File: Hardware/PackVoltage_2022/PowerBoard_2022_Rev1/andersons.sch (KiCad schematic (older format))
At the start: 22 parts

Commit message: Actuation shit
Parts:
- removed unit 3 of Conn2
- removed Conn23: AndersonPP, MRDT_Connectors:Anderson_3_Horizontal_Side_by_Side, symbol PowerBoard_2022_Rev1-rescue:AndersonPP-MRDT_Connectors
- removed unit 3 of Conn3
- removed unit 3 of Conn4
- removed unit 3 of Conn5
- removed unit 3 of Conn6
- removed unit 3 of Conn7
- removed unit 3 of Conn9
- added Conn13: AndersonPP-MRDT_Connectors, MRDT_Connectors:Anderson_3_Horizontal_Side_by_Side, symbol PowerBoard_2022_Rev1-rescue:AndersonPP-MRDT_Connectors
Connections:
- net labels added: Anderson_GimAct, Anderson_SciAct
- net labels removed: Anderson_SciLog
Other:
- moved on the sheet: Conn1C, Conn20A, Conn22B, Conn3A, Conn4A, Conn8C

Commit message: Made it to layout, found out about gnd via
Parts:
- removed Conn13, Conn22: AndersonPP-MRDT_Connectors, MRDT_Connectors:Anderson_3_Horizontal_Side_by_Side, symbol PowerBoard_2022_Rev1-rescue:AndersonPP-MRDT_Connectors
- added unit 2 of Conn11
- added unit 2 of Conn17
- added unit 2 of Conn18
- added unit 2 of Conn19
- added unit 2 of Conn20
- added unit 2 of Conn3
- added unit 2 of Conn4
- added unit 2 of Conn7
- added unit 2 of Conn8
- Conn1, Conn10, Conn11, Conn14, Conn18, Conn4, Conn6, Conn7, Conn8: footprint MRDT_Connectors:Anderson_3_Horizontal_Side_by_Side -> MRDT_Connectors:Anderson_2_Vertical_Sidy_by_Side
- Conn10: renamed from Conn16; footprint MRDT_Connectors:Anderson_3_Horizontal_Side_by_Side -> MRDT_Connectors:Anderson_2_Vertical_Sidy_by_Side
- Conn12, Conn14: renamed from Conn9; footprint MRDT_Connectors:Anderson_3_Horizontal_Side_by_Side -> MRDT_Connectors:Anderson_2_Vertical_Sidy_by_Side
- Conn12, Conn9: renamed from Conn5; footprint MRDT_Connectors:Anderson_3_Horizontal_Side_by_Side -> MRDT_Connectors:Anderson_2_Vertical_Sidy_by_Side
- Conn13, Conn16: renamed from Conn12; footprint MRDT_Connectors:Anderson_3_Horizontal_Side_by_Side -> MRDT_Connectors:Anderson_2_Vertical_Sidy_by_Side
- Conn13: renamed from Conn7; footprint MRDT_Connectors:Anderson_3_Horizontal_Side_by_Side -> MRDT_Connectors:Anderson_2_Vertical_Sidy_by_Side
- Conn15: renamed from Conn17; footprint MRDT_Connectors:Anderson_3_Horizontal_Side_by_Side -> MRDT_Connectors:Anderson_2_Vertical_Sidy_by_Side
- Conn15: renamed from Conn11; footprint MRDT_Connectors:Anderson_3_Horizontal_Side_by_Side -> MRDT_Connectors:Anderson_2_Vertical_Sidy_by_Side
- Conn16: renamed from Conn19; footprint MRDT_Connectors:Anderson_3_Horizontal_Side_by_Side -> MRDT_Connectors:Anderson_2_Vertical_Sidy_by_Side
- Conn17: renamed from Conn15; footprint MRDT_Connectors:Anderson_3_Horizontal_Side_by_Side -> MRDT_Connectors:Anderson_2_Vertical_Sidy_by_Side
- Conn19: renamed from Conn20; footprint MRDT_Connectors:Anderson_3_Horizontal_Side_by_Side -> MRDT_Connectors:Anderson_3_Vertical_Side_by_Side
- Conn19: renamed from Conn8; footprint MRDT_Connectors:Anderson_3_Horizontal_Side_by_Side -> MRDT_Connectors:Anderson_3_Vertical_Side_by_Side
- Conn2: renamed from Conn6; footprint MRDT_Connectors:Anderson_3_Horizontal_Side_by_Side -> MRDT_Connectors:Anderson_2_Vertical_Sidy_by_Side
- Conn2: renamed from Conn4; footprint MRDT_Connectors:Anderson_3_Horizontal_Side_by_Side -> MRDT_Connectors:Anderson_2_Vertical_Sidy_by_Side
- Conn20: renamed from Conn21; footprint MRDT_Connectors:Anderson_3_Horizontal_Side_by_Side -> MRDT_Connectors:Anderson_2_Vertical_Sidy_by_Side
- Conn3: footprint MRDT_Connectors:Anderson_3_Horizontal_Side_by_Side -> MRDT_Connectors:Anderson_3_Vertical_Side_by_Side
- Conn3: renamed from Conn1; footprint MRDT_Connectors:Anderson_3_Horizontal_Side_by_Side -> MRDT_Connectors:Anderson_3_Vertical_Side_by_Side
- Conn5: renamed from Conn2; footprint MRDT_Connectors:Anderson_3_Horizontal_Side_by_Side -> MRDT_Connectors:Anderson_2_Vertical_Sidy_by_Side
- Conn6: renamed from Conn10; footprint MRDT_Connectors:Anderson_3_Horizontal_Side_by_Side -> MRDT_Connectors:Anderson_2_Vertical_Sidy_by_Side
- Conn9: renamed from Conn3; footprint MRDT_Connectors:Anderson_3_Horizontal_Side_by_Side -> MRDT_Connectors:Anderson_2_Vertical_Sidy_by_Side
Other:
- moved on the sheet: Conn10A, Conn10D, Conn12A, Conn12D, Conn13A, Conn13D, Conn14A, Conn14D, Conn15A, Conn15D, Conn16A, Conn16D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

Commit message: Revert "Placed Components for Motor 1 and fixed errors with netlist"
This reverts commit 86a32237b1b6d07fe668dfe10dac6f9ef44dc23b.
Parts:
- Conn1, Conn10, Conn12, Conn13, Conn14, Conn15, Conn16, Conn2, Conn5, Conn6, Conn9: footprint MRDT_Connectors:Anderson_2_Vertical_Sidy_by_Side -> MRDT_Connectors:Anderson_2_Vertical_Side_by_Side_PV
- Conn11, Conn17, Conn18, Conn19, Conn20, Conn3, Conn4, Conn7, Conn8: symbol MRDT_Connectors:AndersonPP -> PowerBoard_2022_Rev1-rescue:AndersonPP-MRDT_Connectors
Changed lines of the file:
@@
 EESchema Schematic File Version 4
-LIBS:PowerBoard_2022_Rev1-cache
-EELAYER 26 0
+EELAYER 30 0
 EELAYER END
 $Descr A4 11693 8268
@@
 F 0 "Conn1" H 808 1837 60  0000 C CNN
 F 1 "AndersonPP" H 808 1731 60  0000 C CNN
-F 2 "MRDT_Connectors:Anderson_2_Vertical_Sidy_by_Side" H 450 900 60  0001 C CNN
+F 2 "MRDT_Connectors:Anderson_2_Vertical_Side_by_Side_PV" H 450 900 60  0001 C CNN
 F 3 "" H 450 900 60  0001 C CNN
 	1    600  1450
@@
 F 0 "Conn1" H 808 1337 60  0000 C CNN
 F 1 "AndersonPP" H 808 1231 60  0000 C CNN
-F 2 "MRDT_Connectors:Anderson_2_Vertical_Sidy_by_Side" H 450 400 60  0001 C CNN
+F 2 "MRDT_Connectors:Anderson_2_Vertical_Side_by_Side_PV" H 450 400 60  0001 C CNN
 F 3 "" H 450 400 60  0001 C CNN
 	4    600  950
@@
 F 0 "Conn9" H 3108 1887 60  0000 C CNN
 F 1 "AndersonPP" H 3108 1781 60  0000 C CNN
-F 2 "MRDT_Connectors:Anderson_2_Vertical_Sidy_by_Side" H 2750 950 60  0001 C CNN
+F 2 "MRDT_Connectors:Anderson_2_Vertical_Side_by_Side_PV" H 2750 950 60  0001 C CNN
 F 3 "" H 2750 950 60  0001 C CNN
 	1    2900 1500
@@
 F 0 "Conn9" H 3108 1387 60  0000 C CNN
 F 1 "AndersonPP" H 3108 1281 60  0000 C CNN
-F 2 "MRDT_Connectors:Anderson_2_Vertical_Sidy_by_Side" H 2750 450 60  0001 C CNN
+F 2 "MRDT_Connectors:Anderson_2_Vertical_Side_by_Side_PV" H 2750 450 60  0001 C CNN
 F 3 "" H 2750 450 60  0001 C CNN
 	4    2900 1000
@@
 F 0 "Conn12" H 4208 1887 60  0000 C CNN
 F 1 "AndersonPP" H 4208 1781 60  0000 C CNN
-F 2 "MRDT_Connectors:Anderson_2_Vertical_Sidy_by_Side" H 3850 950 60  0001 C CNN
+F 2 "MRDT_Connectors:Anderson_2_Vertical_Side_by_Side_PV" H 3850 950 60  0001 C CNN
 F 3 "" H 3850 950 60  0001 C CNN
 	1    4000 1500
@@
 F 0 "Conn12" H 4208 1387 60  0000 C CNN
 F 1 "AndersonPP" H 4208 1281 60  0000 C CNN
-F 2 "MRDT_Connectors:Anderson_2_Vertical_Sidy_by_Side" H 3850 450 60  0001 C CNN
+F 2 "MRDT_Connectors:Anderson_2_Vertical_Side_by_Side_PV" H 3850 450 60  0001 C CNN
 F 3 "" H 3850 450 60  0001 C CNN
 	4    4000 1000
@@
 F 0 "Conn13" H 5258 1887 60  0000 C CNN
 F 1 "AndersonPP" H 5258 1781 60  0000 C CNN
-F 2 "MRDT_Connectors:Anderson_2_Vertical_Sidy_by_Side" H 4900 950 60  0001 C CNN
+F 2 "MRDT_Connectors:Anderson_2_Vertical_Side_by_Side_PV" H 4900 950 60  0001 C CNN
 F 3 "" H 4900 950 60  0001 C CNN
 	1    5050 1500
@@
 F 0 "Conn13" H 5258 1387 60  0000 C CNN
 F 1 "AndersonPP" H 5258 1281 60  0000 C CNN
-F 2 "MRDT_Connectors:Anderson_2_Vertical_Sidy_by_Side" H 4900 450 60  0001 C CNN
+F 2 "MRDT_Connectors:Anderson_2_Vertical_Side_by_Side_PV" H 4900 450 60  0001 C CNN
 F 3 "" H 4900 450 60  0001 C CNN
 	4    5050 1000
@@
 F 0 "Conn14" H 6458 1887 60  0000 C CNN
 F 1 "AndersonPP" H 6458 1781 60  0000 C CNN
-F 2 "MRDT_Connectors:Anderson_2_Vertical_Sidy_by_Side" H 6100 950 60  0001 C CNN
+F 2 "MRDT_Connectors:Anderson_2_Vertical_Side_by_Side_PV" H 6100 950 60  0001 C CNN
 F 3 "" H 6100 950 60  0001 C CNN
 	1    6250 1500
@@
 F 0 "Conn14" H 6458 1387 60  0000 C CNN
 F 1 "AndersonPP" H 6458 1281 60  0000 C CNN
-F 2 "MRDT_Connectors:Anderson_2_Vertical_Sidy_by_Side" H 6100 450 60  0001 C CNN
+F 2 "MRDT_Connectors:Anderson_2_Vertical_Side_by_Side_PV" H 6100 450 60  0001 C CNN
 F 3 "" H 6100 450 60  0001 C CNN
 	4    6250 1000
@@
 F 0 "Conn15" H 7608 1887 60  0000 C CNN
 F 1 "AndersonPP" H 7608 1781 60  0000 C CNN
-F 2 "MRDT_Connectors:Anderson_2_Vertical_Sidy_by_Side" H 7250 950 60  0001 C CNN
+F 2 "MRDT_Connectors:Anderson_2_Vertical_Side_by_Side_PV" H 7250 950 60  0001 C CNN
 F 3 "" H 7250 950 60  0001 C CNN
 	1    7400 1500
@@
 F 0 "Conn15" H 7608 1387 60  0000 C CNN
 F 1 "AndersonPP" H 7608 1281 60  0000 C CNN
-F 2 "MRDT_Connectors:Anderson_2_Vertical_Sidy_by_Side" H 7250 450 60  0001 C CNN
+F 2 "MRDT_Connectors:Anderson_2_Vertical_Side_by_Side_PV" H 7250 450 60  0001 C CNN
 F 3 "" H 7250 450 60  0001 C CNN
 	4    7400 1000
@@
 F 0 "Conn16" H 8858 1887 60  0000 C CNN
 F 1 "AndersonPP" H 8858 1781 60  0000 C CNN
-F 2 "MRDT_Connectors:Anderson_2_Vertical_Sidy_by_Side" H 8500 950 60  0001 C CNN
+F 2 "MRDT_Connectors:Anderson_2_Vertical_Side_by_Side_PV" H 8500 950 60  0001 C CNN
 F 3 "" H 8500 950 60  0001 C CNN
 	1    8650 1500
@@
 F 0 "Conn16" H 8858 1387 60  0000 C CNN
 F 1 "AndersonPP" H 8858 1281 60  0000 C CNN
-F 2 "MRDT_Connectors:Anderson_2_Vertical_Sidy_by_Side" H 8500 450 60  0001 C CNN
+F 2 "MRDT_Connectors:Anderson_2_Vertical_Side_by_Side_PV" H 8500 450 60  0001 C CNN
 F 3 "" H 8500 450 60  0001 C CNN
 	4    8650 1000
@@
 F 0 "Conn5" H 1958 1837 60  0000 C CNN
 F 1 "AndersonPP" H 1958 1731 60  0000 C CNN
-F 2 "MRDT_Connectors:Anderson_2_Vertical_Sidy_by_Side" H 1600 900 60  0001 C CNN
+F 2 "MRDT_Connectors:Anderson_2_Vertical_Side_by_Side_PV" H 1600 900 60  0001 C CNN
 F 3 "" H 1600 900 60  0001 C CNN
 	1    1750 1450
@@
 F 0 "Conn5" H 1958 1337 60  0000 C CNN
 F 1 "AndersonPP" H 1958 1231 60  0000 C CNN
-F 2 "MRDT_Connectors:Anderson_2_Vertical_Sidy_by_Side" H 1600 400 60  0001 C CNN
+F 2 "MRDT_Connectors:Anderson_2_Vertical_Side_by_Side_PV" H 1600 400 60  0001 C CNN
 F 3 "" H 1600 400 60  0001 C CNN
 	4    1750 950
@@
 F 0 "Conn2" H 858 3087 60  0000 C CNN
 F 1 "AndersonPP" H 858 2981 60  0000 C CNN
-F 2 "MRDT_Connectors:Anderson_2_Vertical_Sidy_by_Side" H 500 2150 60  0001 C CNN
+F 2 "MRDT_Connectors:Anderson_2_Vertical_Side_by_Side_PV" H 500 2150 60  0001 C CNN
 F 3 "" H 500 2150 60  0001 C CNN
 	1    650  2700
@@
 F 0 "Conn2" H 858 2587 60  0000 C CNN
 F 1 "AndersonPP" H 858 2481 60  0000 C CNN
-F 2 "MRDT_Connectors:Anderson_2_Vertical_Sidy_by_Side" H 500 1650 60  0001 C CNN
+F 2 "MRDT_Connectors:Anderson_2_Vertical_Side_by_Side_PV" H 500 1650 60  0001 C CNN
 F 3 "" H 500 1650 60  0001 C CNN
 	4    650  2200
@@
 F 0 "Conn6" H 2008 3087 60  0000 C CNN
 F 1 "AndersonPP" H 2008 2981 60  0000 C CNN
-F 2 "MRDT_Connectors:Anderson_2_Vertical_Sidy_by_Side" H 1650 2150 60  0001 C CNN
+F 2 "MRDT_Connectors:Anderson_2_Vertical_Side_by_Side_PV" H 1650 2150 60  0001 C CNN
 F 3 "" H 1650 2150 60  0001 C CNN
 	1    1800 2700
@@
 F 0 "Conn6" H 2008 2587 60  0000 C CNN
 F 1 "AndersonPP" H 2008 2481 60  0000 C CNN
-F 2 "MRDT_Connectors:Anderson_2_Vertical_Sidy_by_Side" H 1650 1650 60  0001 C CNN
+F 2 "MRDT_Connectors:Anderson_2_Vertical_Side_by_Side_PV" H 1650 1650 60  0001 C CNN
 F 3 "" H 1650 1650 60  0001 C CNN
 	4    1800 2200
@@
 F 0 "Conn10" H 3508 3137 60  0000 C CNN
 F 1 "AndersonPP" H 3508 3031 60  0000 C CNN
-F 2 "MRDT_Connectors:Anderson_2_Vertical_Sidy_by_Side" H 3150 2200 60  0001 C CNN
+F 2 "MRDT_Connectors:Anderson_2_Vertical_Side_by_Side_PV" H 3150 2200 60  0001 C CNN
 F 3 "" H 3150 2200 60  0001 C CNN
 	1    3300 2750
@@
 F 0 "Conn10" H 3508 2637 60  0000 C CNN
 F 1 "AndersonPP" H 3508 2531 60  0000 C CNN
-F 2 "MRDT_Connectors:Anderson_2_Vertical_Sidy_by_Side" H 3150 1700 60  0001 C CNN
+F 2 "MRDT_Connectors:Anderson_2_Vertical_Side_by_Side_PV" H 3150 1700 60  0001 C CNN
 F 3 "" H 3150 1700 60  0001 C CNN
 	4    3300 2250
@@
 $EndComp
 $Comp
-L MRDT_Connectors:AndersonPP Conn3
+L PowerBoard_2022_Rev1-rescue:AndersonPP-MRDT_Connectors Conn3
 U 2 1 618FD8B0
 P 950 3550
+AR Path="/618FD8B0" Ref="Conn3"  Part="2"
+AR Path="/615E92DD/618FD8B0" Ref="Conn3"  Part="2"
 F 0 "Conn3" H 1156 3937 60  0000 C CNN
 F 1 "AndersonPP" H 1156 3831 60  0000 C CNN
@@
 $EndComp
 $Comp
-L MRDT_Connectors:AndersonPP Conn7
+L PowerBoard_2022_Rev1-rescue:AndersonPP-MRDT_Connectors Conn7
 U 2 1 618FFBAC
 P 2350 3550
+AR Path="/618FFBAC" Ref="Conn7"  Part="2"
+AR Path="/615E92DD/618FFBAC" Ref="Conn7"  Part="2"
 F 0 "Conn7" H 2556 3937 60  0000 C CNN
 F 1 "AndersonPP" H 2556 3831 60  0000 C CNN
@@
 $EndComp
 $Comp
-L MRDT_Connectors:AndersonPP Conn11
+L PowerBoard_2022_Rev1-rescue:AndersonPP-MRDT_Connectors Conn11
 U 2 1 618FFC14
 P 3750 3550
+AR Path="/618FFC14" Ref="Conn11"  Part="2"
+AR Path="/615E92DD/618FFC14" Ref="Conn11"  Part="2"
 F 0 "Conn11" H 3956 3937 60  0000 C CNN
 F 1 "AndersonPP" H 3956 3831 60  0000 C CNN
@@
 $EndComp
 $Comp
-L MRDT_Connectors:AndersonPP Conn17
+L PowerBoard_2022_Rev1-rescue:AndersonPP-MRDT_Connectors Conn17
 U 2 1 618FFC8E
 P 5250 3550
+AR Path="/618FFC8E" Ref="Conn17"  Part="2"
+AR Path="/615E92DD/618FFC8E" Ref="Conn17"  Part="2"
 F 0 "Conn17" H 5456 3937 60  0000 C CNN
 F 1 "AndersonPP" H 5456 3831 60  0000 C CNN
@@
 $EndComp
 $Comp
-L MRDT_Connectors:AndersonPP Conn18
+L PowerBoard_2022_Rev1-rescue:AndersonPP-MRDT_Connectors Conn18
 U 2 1 618FFD18
 P 6700 3550
+AR Path="/618FFD18" Ref="Conn18"  Part="2"
+AR Path="/615E92DD/618FFD18" Ref="Conn18"  Part="2"
 F 0 "Conn18" H 6906 3937 60  0000 C CNN
 F 1 "AndersonPP" H 6906 3831 60  0000 C CNN
@@
 $EndComp
 $Comp
-L MRDT_Connectors:AndersonPP Conn19
+L PowerBoard_2022_Rev1-rescue:AndersonPP-MRDT_Connectors Conn19
 U 2 1 618FFD90
 P 8200 3550
+AR Path="/618FFD90" Ref="Conn19"  Part="2"
+AR Path="/615E92DD/618FFD90" Ref="Conn19"  Part="2"
 F 0 "Conn19" H 8406 3937 60  0000 C CNN
 F 1 "AndersonPP" H 8406 3831 60  0000 C CNN
@@
 $EndComp
 $Comp
-L MRDT_Connectors:AndersonPP Conn20
+L PowerBoard_2022_Rev1-rescue:AndersonPP-MRDT_Connectors Conn20
 U 2 1 618FFE0A
 P 9800 3550
+AR Path="/618FFE0A" Ref="Conn20"  Part="2"
+AR Path="/615E92DD/618FFE0A" Ref="Conn20"  Part="2"
 F 0 "Conn20" H 10006 3937 60  0000 C CNN
 F 1 "AndersonPP" H 10006 3831 60  0000 C CNN
@@
 $EndComp
 $Comp
-L MRDT_Connectors:AndersonPP Conn4
+L PowerBoard_2022_Rev1-rescue:AndersonPP-MRDT_Connectors Conn4
 U 2 1 618FFE86
 P 950 5200
+AR Path="/618FFE86" Ref="Conn4"  Part="2"
+AR Path="/615E92DD/618FFE86" Ref="Conn4"  Part="2"
 F 0 "Conn4" H 1156 5587 60  0000 C CNN
 F 1 "AndersonPP" H 1156 5481 60  0000 C CNN
@@
 $EndComp
 $Comp
-L MRDT_Connectors:AndersonPP Conn8
+L PowerBoard_2022_Rev1-rescue:AndersonPP-MRDT_Connectors Conn8
 U 2 1 618FFF3E
 P 2800 5250
+AR Path="/618FFF3E" Ref="Conn8"  Part="2"
+AR Path="/615E92DD/618FFF3E" Ref="Conn8"  Part="2"
 F 0 "Conn8" H 3006 5637 60  0000 C CNN
 F 1 "AndersonPP" H 3006 5531 60  0000 C CNN

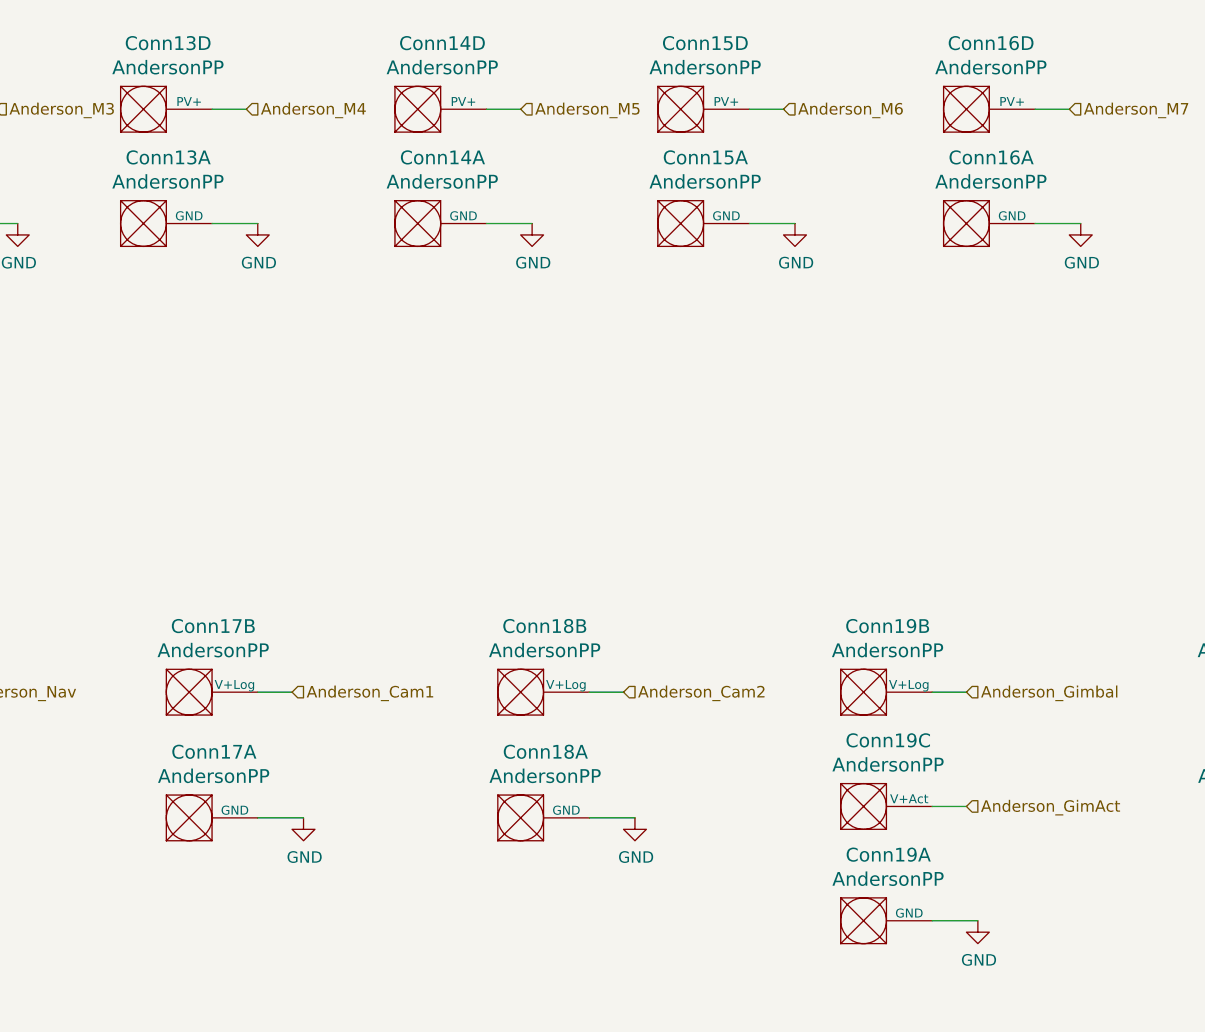
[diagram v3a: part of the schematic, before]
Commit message: Removed redundant LED's in Actuation circuits and final touches on SciAct Layout
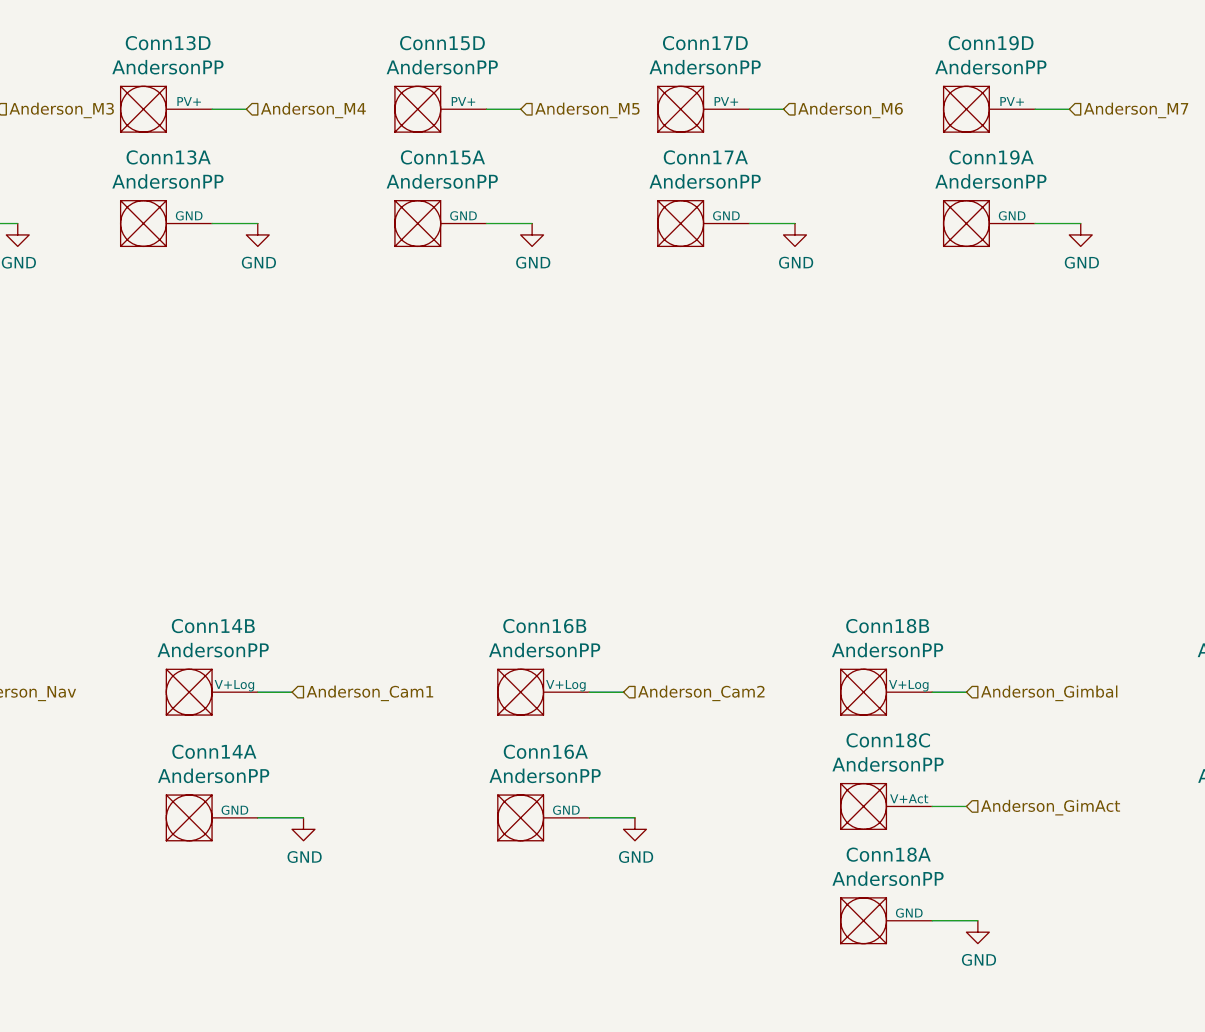
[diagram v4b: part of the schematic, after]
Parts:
- renumbered Conn17 to Conn14, Conn14 to Conn15, Conn18 to Conn16, Conn15 to Conn17, Conn19 to Conn18, Conn16 to Conn19
